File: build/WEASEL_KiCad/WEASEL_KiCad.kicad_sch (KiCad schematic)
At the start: 137 parts, among them J1 MIDI IN, J10 LPG_LEVEL2CTRL, J14 SEQ_OUTPUT2, J15 SEQ_OUTPUT3, J16 EG_OUTPUT1, J17 EG_OUTPUT2, J18 EG_OUTPUT3, J19 PLSR_OUTPUT1, J2 STEREO_OUTPUT, J20 PLSR_OUTPUT2, J21 PLSR_OUTPUT3, J22 RNDM_OUTPUT1, J23 RNDM_OUTPUT2, J24 RNDM_OUTPUT3, J3 SEQ_OUTPUT1, J4 PLSR_PERIODCTRL, J5 MODOSC_FREQCTRL, J6 MODOSC_MODCTRL, J7 COMPOSC_PITCHCTRL, J8 COMPOSC_WAVEFOLDERCTRL, J9 LPG_LEVEL1CTRL, SW1 SQ_TOGGLESTEP1, SW2 SEQ_TRIGGERSELECT, SW3 SQ_TOGGLESTEP2, SW31 EG_TRIGGERSELECT, SW32 EG_MODESELECT, SW33 PLSR_TRIGGERSELECT, SW34 PLSR_MODE, SW35 MODOSC_MIDITOGGLE, SW36 MODOSC_PITCHTRANGE, SW37 COMPLEXOSC_MIDITOGGLE, SW38 COMPLEXOSC_POLARITY, SW39 COMPLEXOSC_WAVETOGGLE, SW4 SQ_TOGGLESTEP3, SW40 LPG_GATE1MODE, SW41 LPG_GATE2MODE, SW42 RNDMVOLTAGE_TRIGGERSELECT, SW43 CLOCK_SYNCTOGGLE, SW5 SQ_TOGGLESTEP4, SW6 SEQ_STAGES, SW7 SQ_TOGGLESTEP5, U1 CD74HC4067, U2 CD74HC4067, U3 6N138

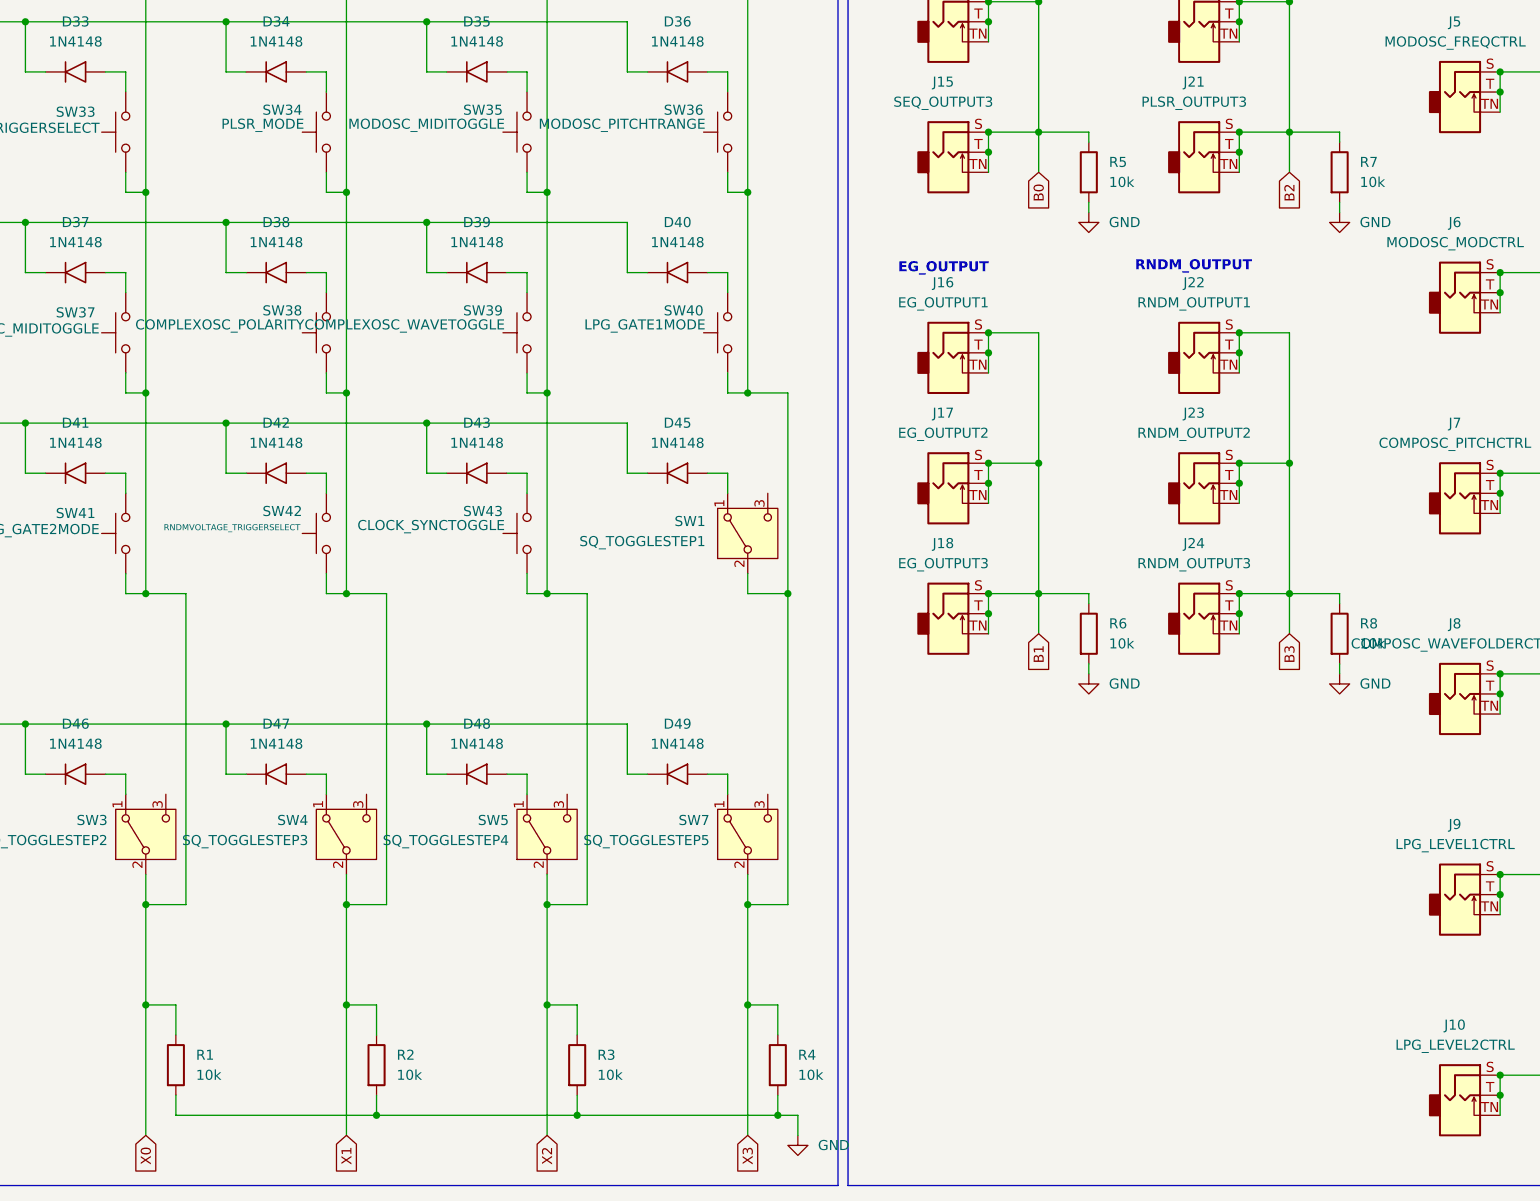
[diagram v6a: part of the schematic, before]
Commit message: PCB & Schematic updates
Created prototype virtual modular matrix
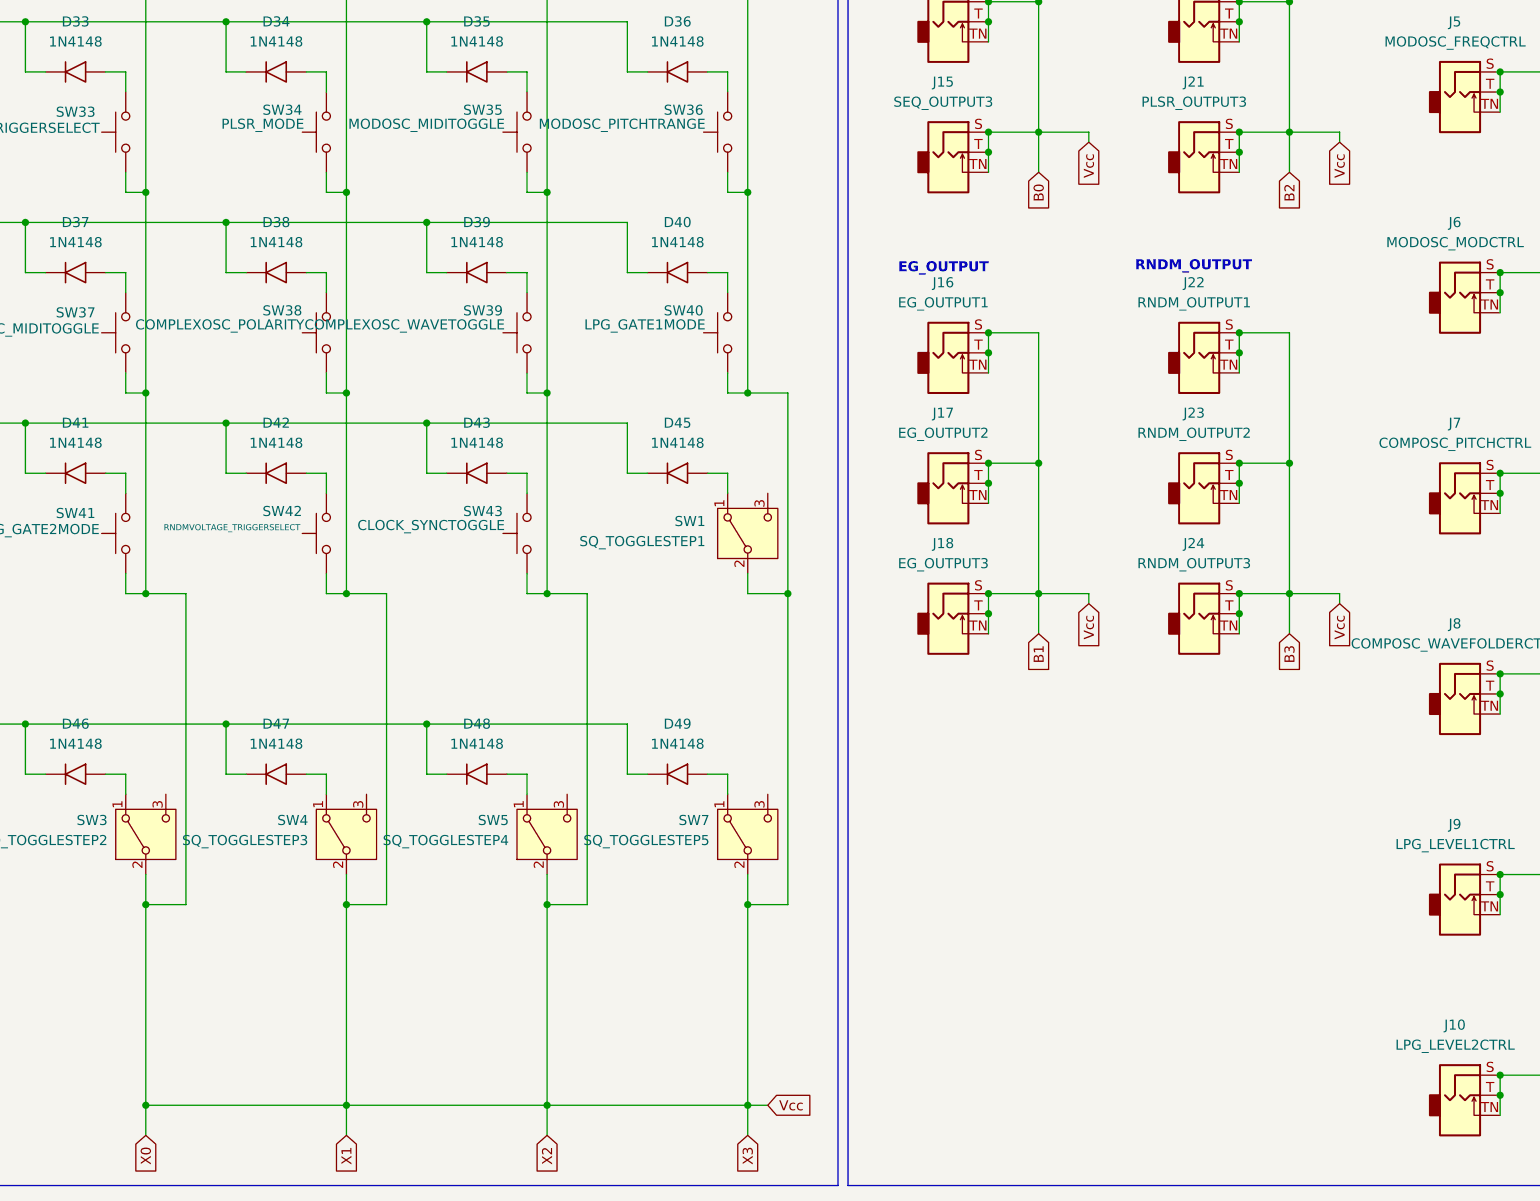
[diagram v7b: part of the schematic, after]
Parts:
- removed R1, R2, R3, R4, R5, R6, R7, R8: 10k, PCM_4ms_Resistor:R_Axial_DIN0207_L6.3mm_D2.5mm_P7.62mm_Horizontal, symbol Device:R
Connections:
- net B1 is gone; now on net B0: A1.27 (ADC_5), J16.S, J16.T, J16.TN, J17.S, J17.T, J17.TN, J18.S, J18.T, J18.TN
- net B2 is gone; now on net B0: A1.28 (ADC_6), J19.S, J19.T, J19.TN, J20.S, J20.T, J20.TN, J21.S, J21.T, J21.TN
- net B3 is gone; now on net B0: A1.29 (DAC_OUT2), J22.S, J22.T, J22.TN, J23.S, J23.T, J23.TN, J24.S, J24.T, J24.TN
- net Vcc is gone; now on net B0: A1.38 (3V3_D), R9.1, RV1.3, RV10.3, RV11.3, RV12.1, RV13.3, RV14.3, RV15.3, RV16.3, RV17.3, RV18.3, RV19.3, RV2.3, RV20.3, RV21.3, RV22.3, RV23.3, RV24.3, RV25.3, RV26.3, RV27.3, RV3.3, RV4.3, RV5.3, RV6.3, RV7.3, RV8.3, RV9.3, U1.24 (vcc), U2.24 (vcc), U3.8 (VCC)
- net X0 is gone; now on net B0: A1.13 (I2C1_SDA), SW2.1, SW3.2 (B), SW33.1, SW37.1, SW41.1
- net X1 is gone; now on net B0: A1.14 (USART1_TX), SW34.1, SW38.1, SW4.2 (B), SW42.1, SW6.1
- net X2 is gone; now on net B0: A1.24 (ADC_2), SW31.1, SW35.1, SW39.1, SW43.1, SW5.2 (B)
- net X3 is gone; now on net B0: A1.25 (ADC_3), SW1.2 (B), SW32.1, SW36.1, SW40.1, SW7.2 (B)

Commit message: PCB & Schematic update
- Removed unnecessary capacitors for each pot. Each MUX signal pin has a capacitor to filter the signal.
- New board layout
- More compact and organised.
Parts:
- removed C10, C11, C12, C13, C14, C15, C16, C17, C18, C19, C20, C21, C22, C23, C24, C25, C26, C27, C3, C4, C5, C6, C7, C8, C9: 10nF, DIYSynthMNL:C_Rect_L7.0mm_W2.0mm_P5.00mm_BigPads, symbol Device:C
- C1, C2: footprint DIYSynthMNL:C_Rect_L7.0mm_W2.0mm_P5.00mm_BigPads -> PCM_4ms_Capacitor:C_Disc_P5.08mm
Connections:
- net B0: no longer A1.13 (I2C1_SDA), A1.14 (USART1_TX), A1.24 (ADC_2), A1.25 (ADC_3), A1.27 (ADC_5), A1.28 (ADC_6), A1.29 (DAC_OUT2), A1.38 (3V3_D), J16.S, J16.T, J16.TN, J17.S, J17.T, J17.TN, J18.S, J18.T, J18.TN, J19.S, J19.T, J19.TN, J20.S, J20.T, J20.TN, J21.S, J21.T, J21.TN, J22.S, J22.T, J22.TN, J23.S, J23.T, J23.TN, J24.S, J24.T, J24.TN, R9.1, RV1.3, RV10.3, RV11.3, RV12.1, RV13.3, RV14.3, RV15.3, RV16.3, RV17.3, RV18.3, RV19.3, RV2.3, RV20.3, RV21.3, RV22.3, RV23.3, RV24.3, RV25.3, RV26.3, RV27.3, RV3.3, RV4.3, RV5.3, RV6.3, RV7.3, RV8.3, RV9.3, SW1.2 (B), SW2.1, SW3.2 (B), SW31.1, SW32.1, SW33.1, SW34.1, SW35.1, SW36.1, SW37.1, SW38.1, SW39.1, SW4.2 (B), SW40.1, SW41.1, SW42.1, SW43.1, SW5.2 (B), SW6.1, SW7.2 (B), U1.24 (vcc), U2.24 (vcc), U3.8 (VCC)
- net MUX1_SIGNAL: now also C1.1
- net MUX2_SIGNAL: now also C2.1
- net at RV2.2, U1.8 (i1): no longer C2.1
- net at RV1.2, U1.9 (i0): no longer C1.1
- new net B1: A1.27 (ADC_5), J16.S, J16.T, J16.TN, J17.S, J17.T, J17.TN, J18.S, J18.T, J18.TN
- new net B2: A1.28 (ADC_6), J19.S, J19.T, J19.TN, J20.S, J20.T, J20.TN, J21.S, J21.T, J21.TN
- new net B3: A1.29 (DAC_OUT2), J22.S, J22.T, J22.TN, J23.S, J23.T, J23.TN, J24.S, J24.T, J24.TN
- new net Vcc: A1.38 (3V3_D), R9.1, RV1.3, RV10.3, RV11.3, RV12.1, RV13.3, RV14.3, RV15.3, RV16.3, RV17.3, RV18.3, RV19.3, RV2.3, RV20.3, RV21.3, RV22.3, RV23.3, RV24.3, RV25.3, RV26.3, RV27.3, RV3.3, RV4.3, RV5.3, RV6.3, RV7.3, RV8.3, RV9.3, U1.24 (vcc), U2.24 (vcc), U3.8 (VCC)
- new net X0: A1.13 (I2C1_SDA), SW2.1, SW3.2 (B), SW33.1, SW37.1, SW41.1
- new net X1: A1.14 (USART1_TX), SW34.1, SW38.1, SW4.2 (B), SW42.1, SW6.1
- new net X2: A1.24 (ADC_2), SW31.1, SW35.1, SW39.1, SW43.1, SW5.2 (B)
- new net X3: A1.25 (ADC_3), SW1.2 (B), SW32.1, SW36.1, SW40.1, SW7.2 (B)
